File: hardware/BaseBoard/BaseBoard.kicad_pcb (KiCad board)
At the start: 2 copper layers, 81.3 x 106.7 mm, 79 parts, among them IC1 PCF8574RGTR, J1-ESP1 ESP-1-L, J1-ESP2 ESP-1-L, J1-ESP3 ESP-1-L, J1-ESP4 ESP-1-L, J1-ESP5 ESP-1-L, J1-ESP6 ESP-1-L, J1-ESP7 ESP-1-L, J1-ESP8 ESP-1-L, J2-ESP1 ESP-1-R, J2-ESP2 ESP-1-R, J2-ESP3 ESP-1-R, J2-ESP4 ESP-1-R, J2-ESP5 ESP-1-R, J2-ESP6 ESP-1-R, J2-ESP7 ESP-1-R, J2-ESP8 ESP-1-R, J3-BUS1 BUS-IN, J3-BUS2 BUS-IN, J3-BUS3 BUS-IN, J3-BUS4 BUS-IN, J3-BUS5 BUS-IN, J3-BUS6 BUS-IN, J3-BUS7 BUS-IN, J3-BUS8 BUS-IN, J4-BUS1 BUS-OUT, J4-BUS2 BUS-OUT, J4-BUS3 BUS-OUT, J4-BUS4 BUS-OUT, J4-BUS5 BUS-OUT, J4-BUS6 BUS-OUT, J4-BUS7 BUS-OUT, J4-BUS8 BUS-OUT, Q1 AO3401A, Q2 AO3401A, Q3 AO3401A, Q4 AO3401A, Q5 AO3401A, Q6 AO3401A, Q7 AO3401A, Q8 AO3401A, SW1 SW_DIP_SPSTx03

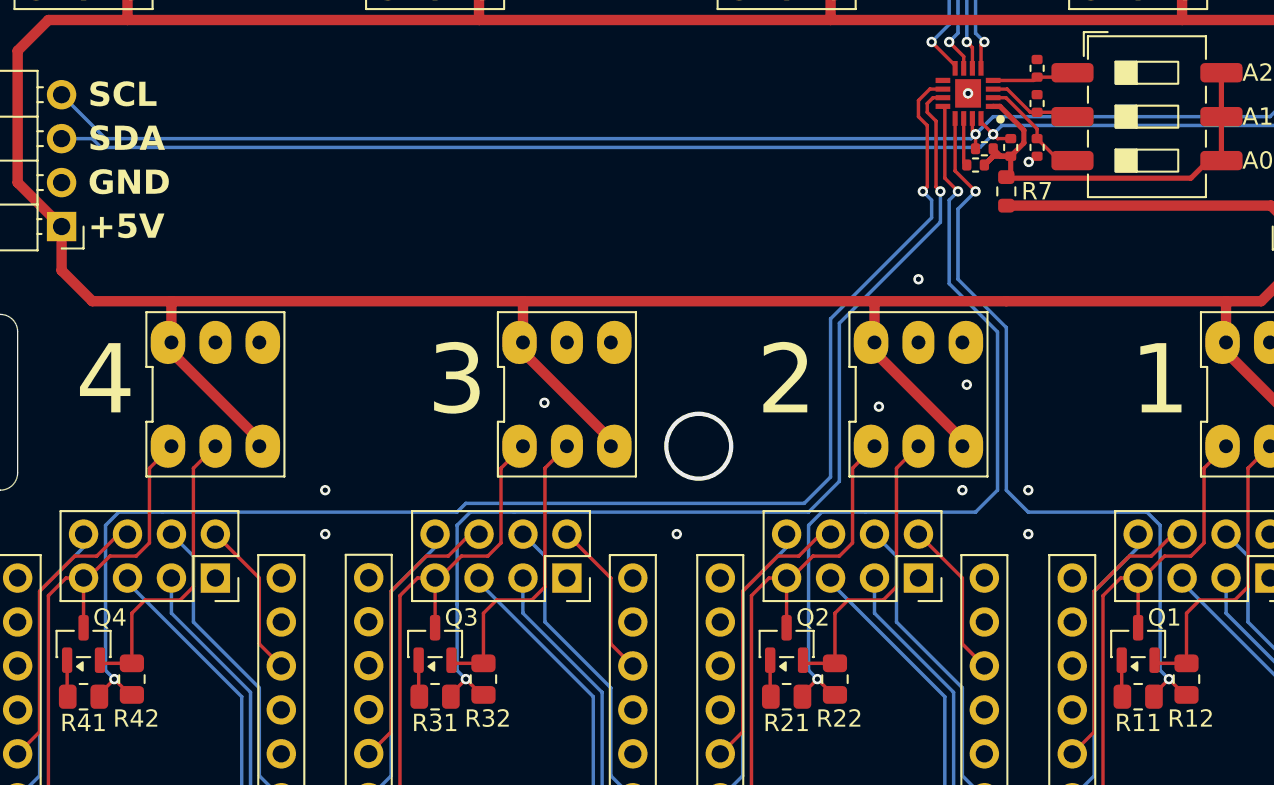
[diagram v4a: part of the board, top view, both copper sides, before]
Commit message: Removed pull-up resistors for I2C slaves.
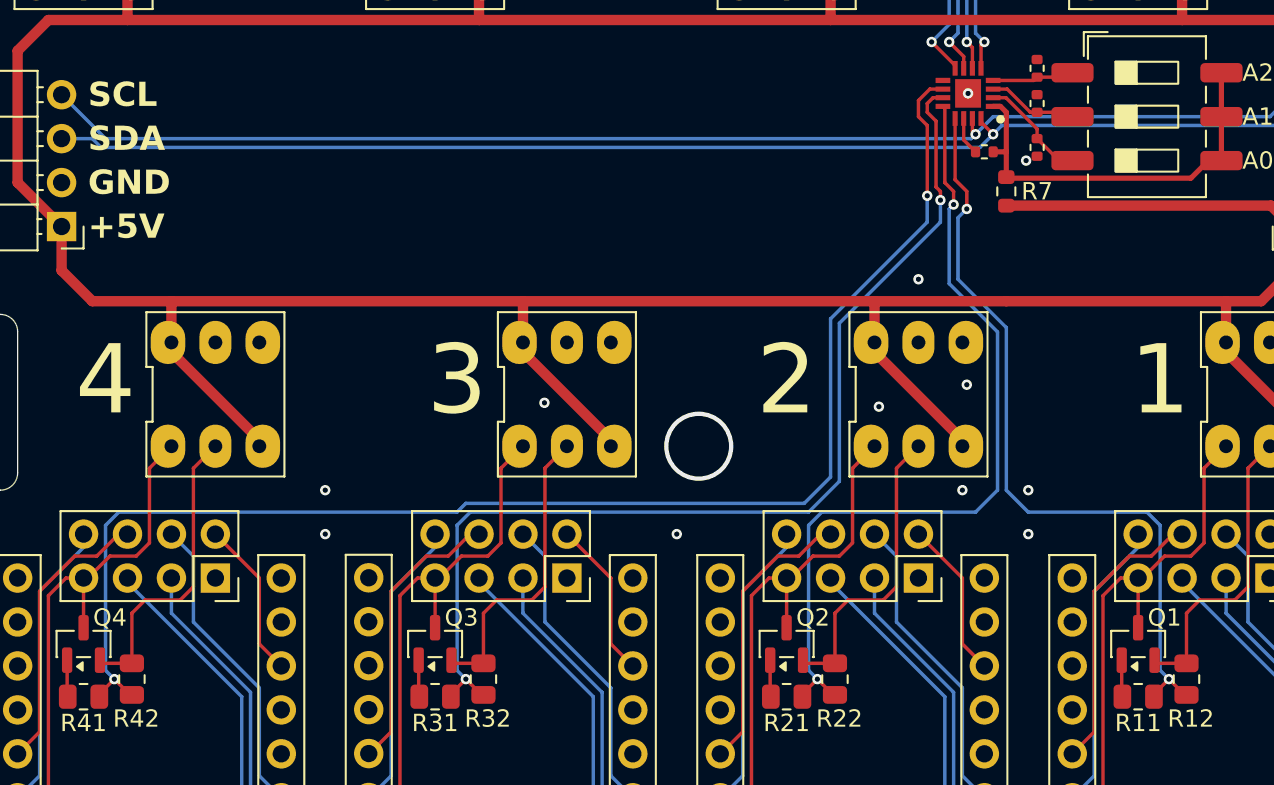
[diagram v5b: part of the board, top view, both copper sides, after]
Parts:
- removed R1, R2: 10k, Resistor_SMD:R_0402_1005Metric
- moved R3 0.92 mm to (180.3, 71.9)
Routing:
- net +5VSwitching: track 27.5 -> 23.4 mm
- net I2C_SDA: track 74.5 -> 73.4 mm
- net I2C_SCL: track 75.0 -> 74.2 mm
- net INT: track 2.76 -> 2.21 mm

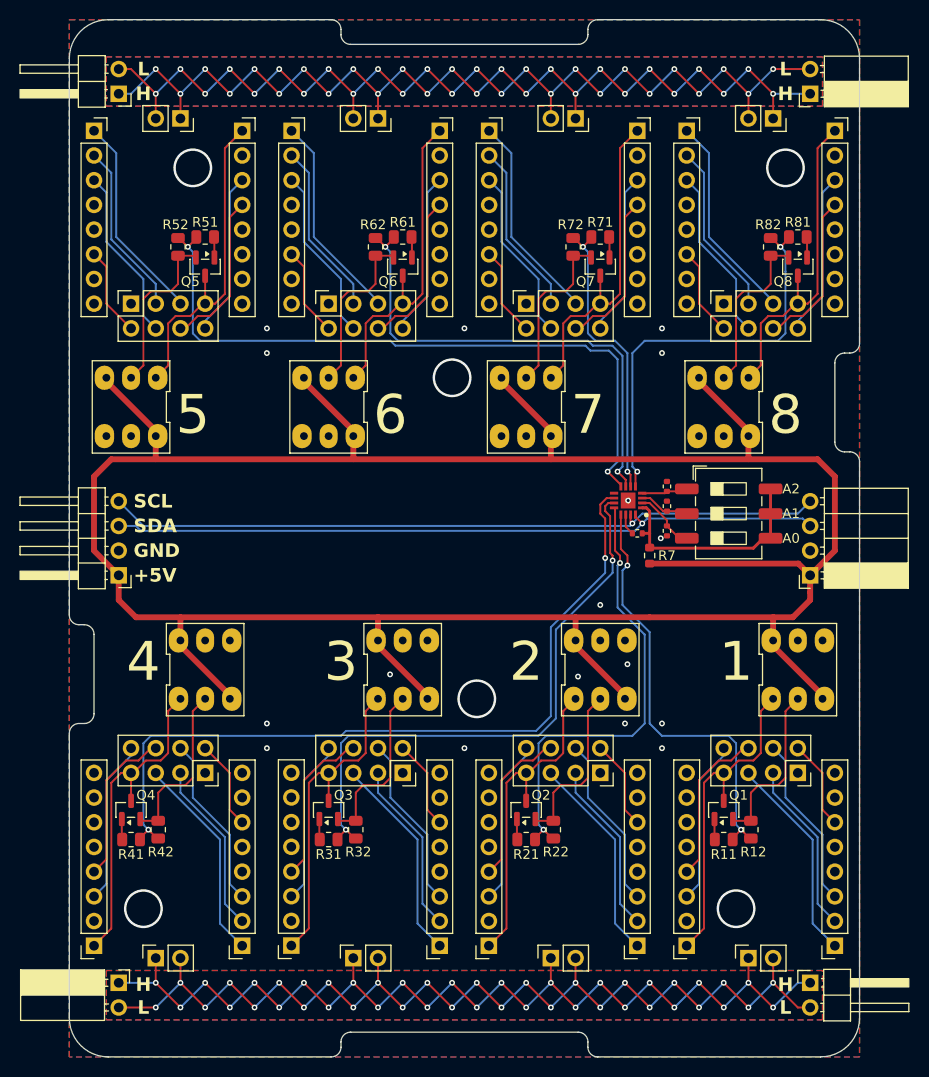
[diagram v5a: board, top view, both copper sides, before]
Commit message: Added diodes to base board.
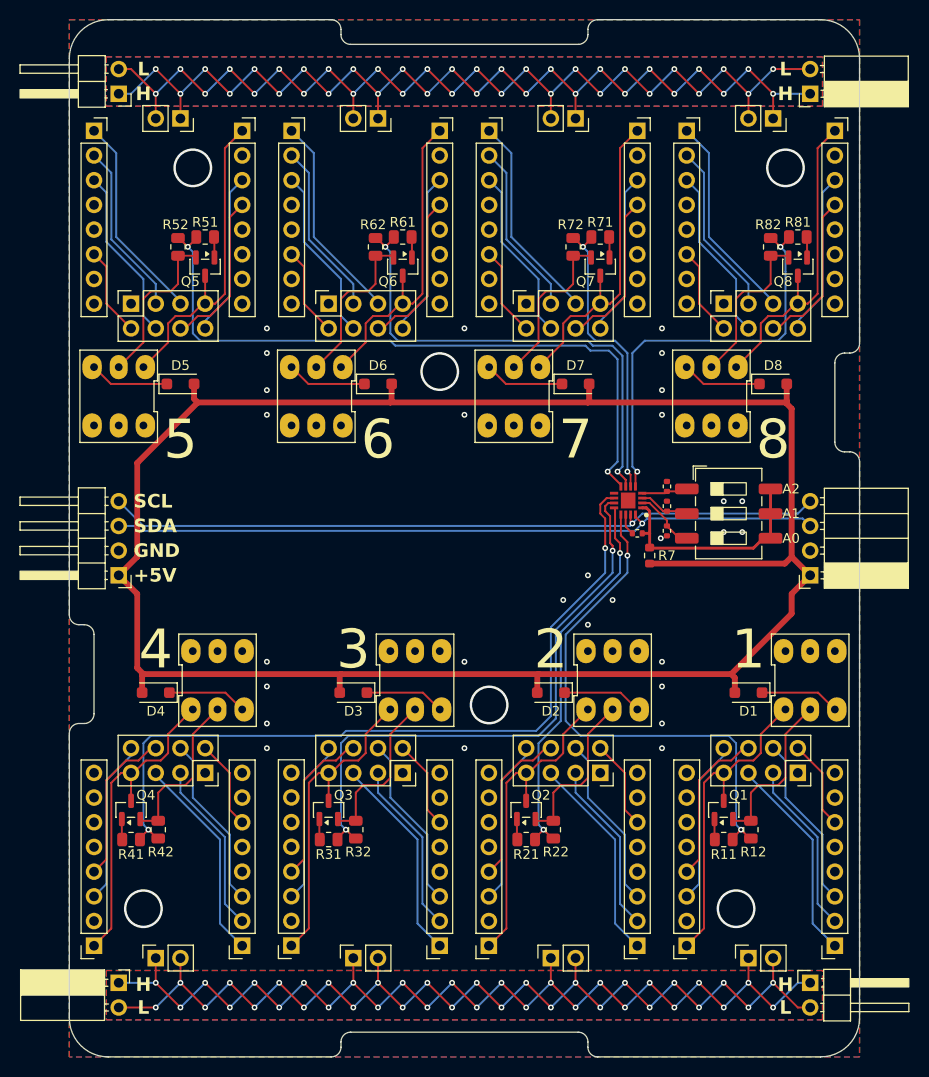
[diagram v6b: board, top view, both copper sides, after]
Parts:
- added D1: MBR1020VL, Diode_SMD:D_SOD-123F, F.Cu at (191.8, 88.3)
- added D2: MBR1020VL, Diode_SMD:D_SOD-123F, F.Cu at (171.4, 88.3)
- added D3: MBR1020VL, Diode_SMD:D_SOD-123F, F.Cu at (151.1, 88.3)
- added D4: MBR1020VL, Diode_SMD:D_SOD-123F, F.Cu at (130.8, 88.3)
- added D5: MBR1020VL, Diode_SMD:D_SOD-123F, F.Cu at (133.3, 56.5)
- added D6: MBR1020VL, Diode_SMD:D_SOD-123F, F.Cu at (153.7, 56.5)
- added D7: MBR1020VL, Diode_SMD:D_SOD-123F, F.Cu at (174.0, 56.5)
- added D8: MBR1020VL, Diode_SMD:D_SOD-123F, F.Cu at (194.3, 56.5)
- moved ESP5 1.68 mm to (127.0, 57.8)
- moved ESP6 1.68 mm to (147.3, 57.8)
- moved ESP7 1.68 mm to (167.6, 57.8)
- moved ESP1 1.68 mm to (198.1, 87.0)
- moved ESP2 1.68 mm to (177.8, 87.0)
- moved ESP4 1.68 mm to (137.2, 87.0)
- moved ESP8 1.68 mm to (188.0, 57.8)
- moved ESP3 1.68 mm to (157.5, 87.0)
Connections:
- ESP1 pad 3: +5V -> Net-(D1-K)
- ESP1 pad 6: +5V -> unconnected-(ESP1-Pad6)
- ESP2 pad 3: +5V -> Net-(D2-K)
- ESP2 pad 6: +5V -> unconnected-(ESP2-Pad6)
- ESP3 pad 3: +5V -> Net-(D3-K)
- ESP3 pad 6: +5V -> unconnected-(ESP3-Pad6)
- ESP4 pad 3: +5V -> Net-(D4-K)
- ESP4 pad 6: +5V -> unconnected-(ESP4-Pad6)
- ESP5 pad 3: +5V -> Net-(D5-K)
- ESP5 pad 6: +5V -> unconnected-(ESP5-Pad6)
- ESP6 pad 3: +5V -> Net-(D6-K)
- ESP6 pad 6: +5V -> unconnected-(ESP6-Pad6)
- ESP7 pad 3: +5V -> Net-(D7-K)
- ESP7 pad 6: +5V -> unconnected-(ESP7-Pad6)
- ESP8 pad 3: +5V -> Net-(D8-K)
- ESP8 pad 6: +5V -> unconnected-(ESP8-Pad6)
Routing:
- net +5V: track 278.8 -> 216.5 mm
- net SWPIN-ESP1: track 44.7 -> 54.5 mm
- net Net-(D6-K): track 0.00 -> 8.21 mm
- net Net-(D2-K): track 0.00 -> 8.21 mm
- net Net-(D1-K): track 0.00 -> 8.21 mm
- net Net-(D8-K): track 0.00 -> 8.21 mm
- net Net-(D7-K): track 0.00 -> 8.21 mm
- net Net-(D3-K): track 0.00 -> 8.21 mm
- net Net-(D5-K): track 0.00 -> 8.21 mm
- net Net-(D4-K): track 0.00 -> 8.21 mm
- net SWPIN-ESP2: track 47.3 -> 39.8 mm
- net Net-(Q8-S): track 17.7 -> 17.1 mm
- net Net-(J2-ESP7-Pin_1): track 33.6 -> 33.0 mm
- net Net-(J2-ESP6-Pin_1): track 33.6 -> 33.0 mm
- net Net-(Q3-S): track 17.7 -> 17.1 mm
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
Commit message: Added capacitors for +3V3 stabilization.
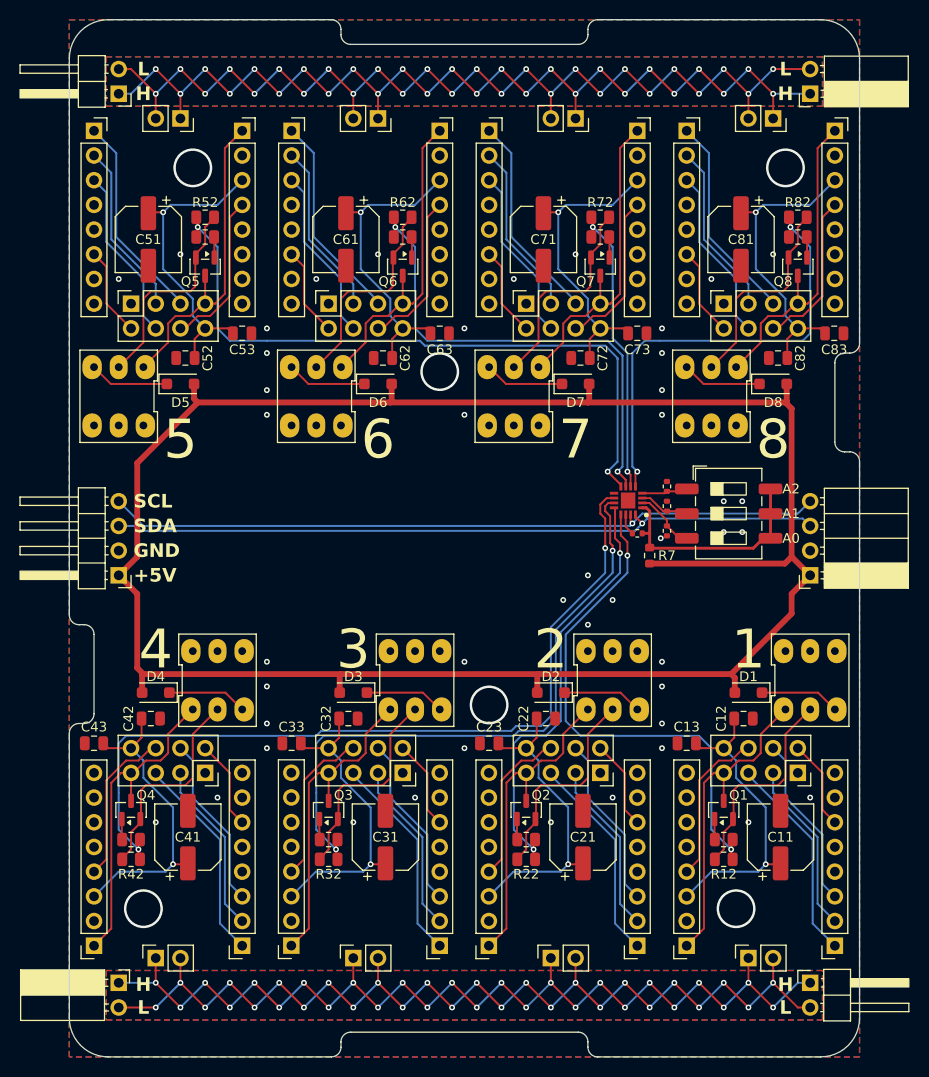
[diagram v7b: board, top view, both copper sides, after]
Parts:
- added C11: 220µF, Capacitor_SMD:CP_Elec_6.3x7.7, F.Cu at (195.1, 103.1)
- added C12: 47µF, Capacitor_SMD:C_0805_2012Metric, F.Cu at (191.3, 90.9)
- added C13: 47µF, Capacitor_SMD:C_0805_2012Metric, F.Cu at (185.4, 93.5)
- added C21: 220µF, Capacitor_SMD:CP_Elec_6.3x7.7, F.Cu at (174.8, 103.1)
- added C22: 47µF, Capacitor_SMD:C_0805_2012Metric, F.Cu at (170.9, 90.9)
- added C23: 47µF, Capacitor_SMD:C_0805_2012Metric, F.Cu at (165.1, 93.5)
- added C31: 220µF, Capacitor_SMD:CP_Elec_6.3x7.7, F.Cu at (154.4, 103.1)
- added C32: 47µF, Capacitor_SMD:C_0805_2012Metric, F.Cu at (150.6, 90.9)
- added C33: 47µF, Capacitor_SMD:C_0805_2012Metric, F.Cu at (144.8, 93.5)
- added C41: 220µF, Capacitor_SMD:CP_Elec_6.3x7.7, F.Cu at (134.1, 103.1)
- added C42: 47µF, Capacitor_SMD:C_0805_2012Metric, F.Cu at (130.3, 90.9)
- added C43: 47µF, Capacitor_SMD:C_0805_2012Metric, F.Cu at (124.5, 93.5)
- added C51: 220µF, Capacitor_SMD:CP_Elec_6.3x7.7, F.Cu at (130.0, 41.7)
- added C52: 47µF, Capacitor_SMD:C_0805_2012Metric, F.Cu at (133.9, 53.8)
- added C53: 47µF, Capacitor_SMD:C_0805_2012Metric, F.Cu at (139.7, 51.3)
- added C61: 220µF, Capacitor_SMD:CP_Elec_6.3x7.7, F.Cu at (150.4, 41.7)
- added C62: 47µF, Capacitor_SMD:C_0805_2012Metric, F.Cu at (154.2, 53.8)
- added C63: 47µF, Capacitor_SMD:C_0805_2012Metric, F.Cu at (160.0, 51.3)
- added C71: 220µF, Capacitor_SMD:CP_Elec_6.3x7.7, F.Cu at (170.7, 41.7)
- added C72: 47µF, Capacitor_SMD:C_0805_2012Metric, F.Cu at (174.5, 53.8)
- added C73: 47µF, Capacitor_SMD:C_0805_2012Metric, F.Cu at (180.3, 51.3)
- added C81: 220µF, Capacitor_SMD:CP_Elec_6.3x7.7, F.Cu at (191.0, 41.7)
- added C82: 47µF, Capacitor_SMD:C_0805_2012Metric, F.Cu at (194.8, 53.8)
- added C83: 47µF, Capacitor_SMD:C_0805_2012Metric, F.Cu at (200.6, 51.3)
- moved R12 4.13 mm to (189.2, 105.4), turned to 0 degrees
- moved R22 4.13 mm to (168.9, 105.4), turned to 0 degrees
- moved R62 4.13 mm to (156.2, 39.4), turned to 180 degrees
- moved R72 4.13 mm to (176.5, 39.4), turned to 180 degrees
- moved R32 4.13 mm to (148.6, 105.4), turned to 0 degrees
- moved R42 4.13 mm to (128.3, 105.4), turned to 0 degrees
- moved R52 4.13 mm to (135.9, 39.4), turned to 180 degrees
- moved R82 4.13 mm to (196.8, 39.4), turned to 180 degrees
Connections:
- net Net-(J2-ESP1-Pin_3) renamed +3V3-ESP1
- net Net-(J2-ESP2-Pin_3) renamed +3V3-ESP2
- net Net-(J2-ESP3-Pin_3) renamed +3V3-ESP3
- net Net-(J2-ESP4-Pin_3) renamed +3V3-ESP4
- net Net-(J2-ESP5-Pin_3) renamed +3V3-ESP5
- net Net-(J2-ESP6-Pin_3) renamed +3V3-ESP6
- net Net-(J2-ESP7-Pin_3) renamed +3V3-ESP7
- net Net-(J2-ESP8-Pin_3) renamed +3V3-ESP8
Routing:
- net +3V3-ESP2: track 17.6 -> 32.1 mm, vias 0 -> 1
- net +3V3-ESP3: track 16.8 -> 31.4 mm, vias 0 -> 1
- net +3V3-ESP1: track 16.8 -> 31.4 mm, vias 0 -> 1
- net +3V3-ESP6: track 16.8 -> 31.4 mm, vias 0 -> 1
- net +3V3-ESP7: track 16.8 -> 31.4 mm, vias 0 -> 1
- net +3V3-ESP4: track 16.8 -> 31.4 mm, vias 0 -> 1
- net +3V3-ESP5: track 16.8 -> 31.4 mm, vias 0 -> 1
- net +3V3-ESP8: track 16.8 -> 31.3 mm, vias 0 -> 1
- net Net-(Q1-S): track 17.1 -> 22.1 mm
- net Net-(Q6-S): track 17.1 -> 21.9 mm
- net Net-(Q5-S): track 17.1 -> 21.9 mm
- net Net-(Q2-S): track 17.1 -> 21.9 mm
- net Net-(Q8-S): track 17.1 -> 21.9 mm
- net Net-(Q7-S): track 17.1 -> 21.9 mm
- net Net-(Q4-S): track 17.1 -> 21.9 mm
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
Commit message: Improved isolation of bus connections.
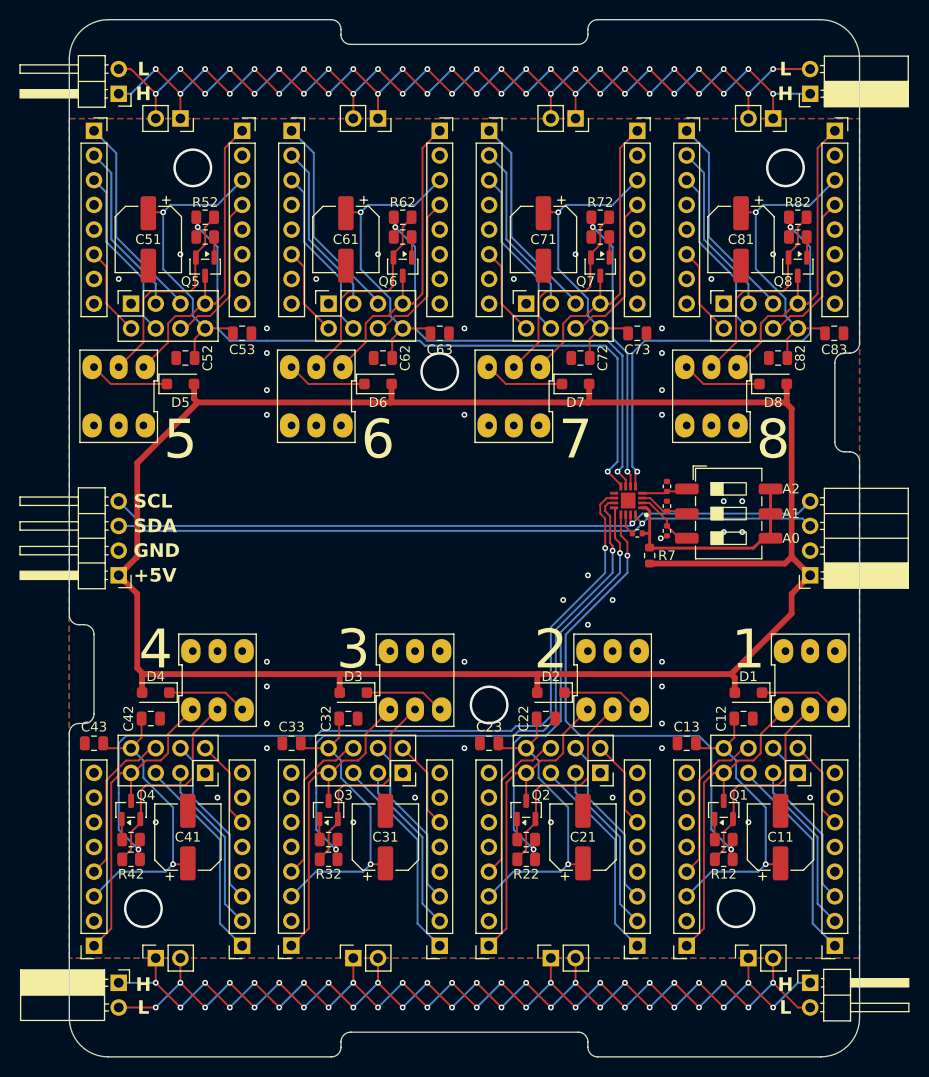
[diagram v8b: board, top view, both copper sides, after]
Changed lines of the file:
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@@
 		(net 3)
 		(net_name "GNDREF")
-		(layer "F.Cu")
+		(layers "F.Cu" "B.Cu")
 		(hatch edge 0.5)
 		(connect_pads yes
@@
 		(polygon
 			(pts
-				(xy 203.2 125.741006) (xy 121.92 125.741006) (xy 121.92 19.061006) (xy 203.2 19.061006)
+				(xy 203.2 115.581006) (xy 121.92 115.581006) (xy 121.92 29.221006) (xy 203.2 29.221006)
 			)
 		)
-		(polygon
-			(pts
-				(xy 125.73 116.851006) (xy 125.73 121.931006) (xy 199.39 121.931006) (xy 199.39 116.851006)
-			)
-		)
-		(polygon
-			(pts
-				(xy 125.73 27.951006) (xy 199.39 27.951006) (xy 199.39 22.871006) (xy 125.73 22.871006)
-			)
-		)
-	)
-	(zone
-		(net 3)
-		(net_name "GNDREF")
-		(layer "B.Cu")
-		(hatch edge 0.5)
-		(priority 1)
-		(connect_pads yes
-			(clearance 0.5)
-		)
-		(min_thickness 0.25)
-		(filled_areas_thickness no)
-		(fill yes
-			(thermal_gap 0.5)
-			(thermal_bridge_width 0.5)
-		)
-		(polygon
-			(pts
-				(xy 203.2 125.73) (xy 121.92 125.73) (xy 121.92 19.05) (xy 203.2 19.05)
-			)
-		)
-		(polygon
-			(pts
-				(xy 125.73 121.92) (xy 199.39 121.92) (xy 199.39 116.84) (xy 125.73 116.84)
-			)
-		)
-		(polygon
-			(pts
-				(xy 125.73 22.86) (xy 125.73 27.94) (xy 199.39 27.94) (xy 199.39 22.86)
-			)
-		)
